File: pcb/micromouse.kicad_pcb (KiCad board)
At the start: 2 copper layers, 50 x 79.6 mm, 14 parts, among them J1 AVR-ISP-6, U1 TSSP77038ETR, U2 TSSP77038ETR, U3 TSSP77038ETR, U4 TSSP77038ETR, U5 TSSP77038ETR, U6 TSSP77038ETR, U7 ATmega328PB-A, Y1 Crystal

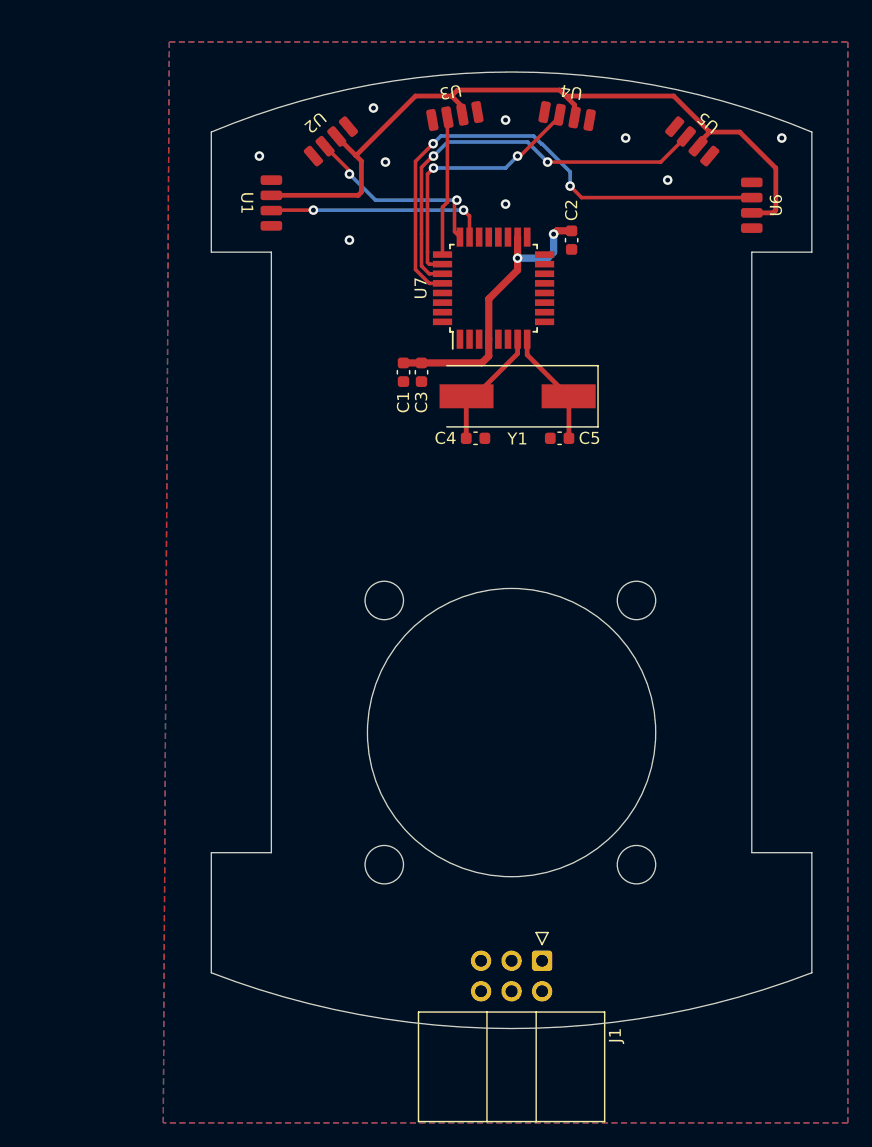
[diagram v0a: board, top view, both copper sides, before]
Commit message: add IR 3d + pin i2c screen
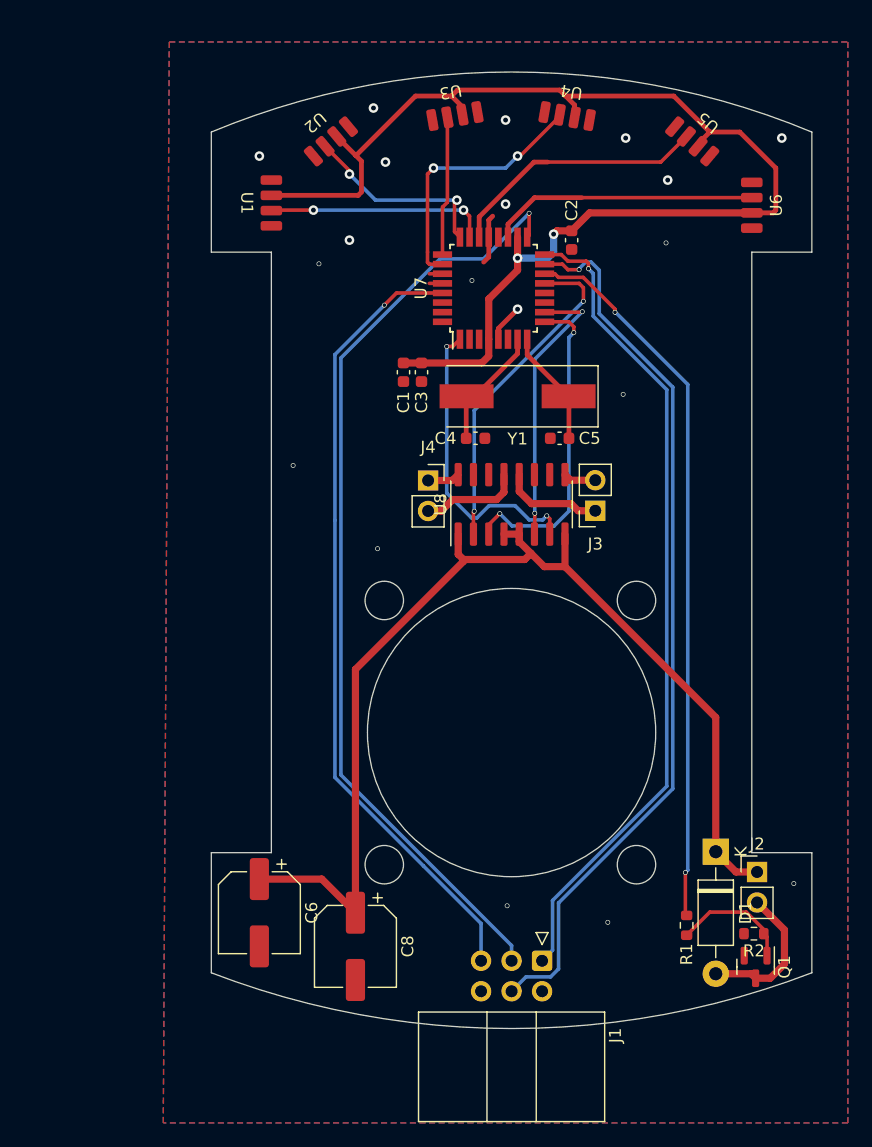
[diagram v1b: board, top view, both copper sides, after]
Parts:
- added C6: C_Polarized_Small, Capacitor_SMD:CP_Elec_6.3x4.9, F.Cu at (104.0, 95.0)
- added C8: C_Polarized_Small, Capacitor_SMD:CP_Elec_6.3x4.9, F.Cu at (112.0, 97.8)
- added D1: 1N5819, Diode_THT:D_DO-41_SOD81_P10.16mm_Horizontal, F.Cu at (142.0, 89.9)
- added J2: Conn_01x02, Connector_PinHeader_2.54mm:PinHeader_1x02_P2.54mm_Vertical, F.Cu at (145.4, 91.6)
- added J3: Conn_01x02, Connector_PinSocket_2.54mm:PinSocket_1x02_P2.54mm_Vertical, F.Cu at (132.0, 61.5)
- added J4: Conn_01x02, Connector_PinSocket_2.54mm:PinSocket_1x02_P2.54mm_Vertical, F.Cu at (118.0, 59.0)
- added Q1: Si2319CDS, Package_TO_SOT_SMD:SOT-23, F.Cu at (145.3, 99.5)
- added R1: R_Small, Resistor_SMD:R_0603_1608Metric, F.Cu at (139.6, 96.0)
- added R2: R_Small, Resistor_SMD:R_0603_1608Metric, F.Cu at (145.2, 96.7)
- added U8: MX1508, Package_SO:SOIC-16_3.9x9.9mm_P1.27mm, F.Cu at (125.0, 61.0)
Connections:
- U7 pad 14: unconnected-(U7-PB2-Pad14) -> MOTOR_1
- U7 pad 19: unconnected-(U7-PE2-Pad19) -> IR6
- U7 pad 22: unconnected-(U7-PE3-Pad22) -> IR5
- U7 pad 27: IR5 -> SDA
- U7 pad 28: IR6 -> SCL
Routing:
- net +BATT: track 0.00 -> 92.8 mm
- net SCK: track 0.00 -> 78.8 mm, vias 0 -> 1
- net MOSI: track 0.00 -> 74.7 mm, vias 0 -> 1
- net MISO: track 0.00 -> 69.0 mm, vias 0 -> 1
- net RST: track 0.00 -> 66.6 mm, vias 0 -> 1
- net MOTOR_1: track 0.00 -> 60.2 mm, vias 0 -> 2
- net MTR_L_1: track 0.00 -> 27.7 mm, vias 0 -> 2
- net MTR_L_2: track 0.00 -> 26.9 mm, vias 0 -> 2
- net MTR_R_2: track 0.00 -> 25.4 mm, vias 0 -> 2
- net MTR_R_1: track 0.00 -> 23.3 mm, vias 0 -> 2
- net IR6: track 43.4 -> 22.3 mm, vias 2 -> 0
- net +3.3V: track 88.8 -> 104.4 mm
- net IR5: track 34.7 -> 21.7 mm, vias 2 -> 0
- net Net-(D1-A): track 0.00 -> 12.4 mm
- net Net-(Q1-G): track 0.00 -> 10.1 mm
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
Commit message: remake IR wiring
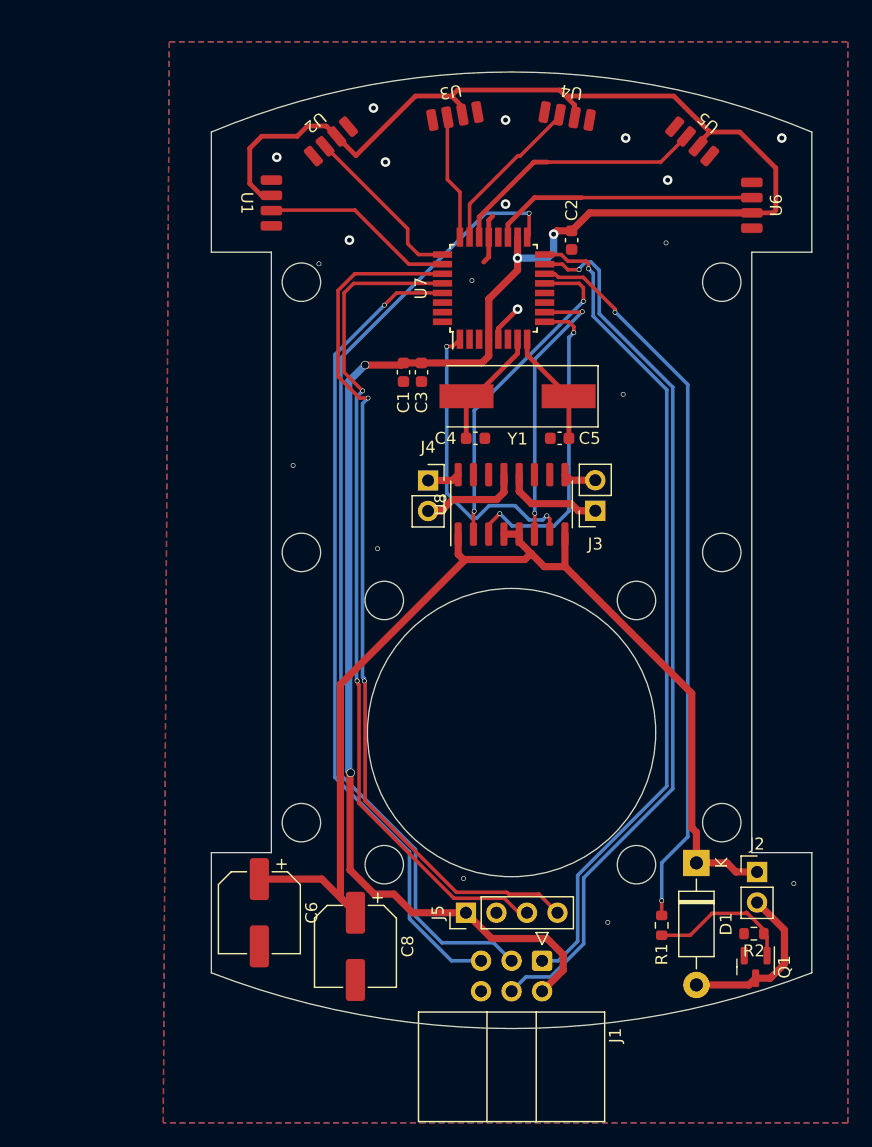
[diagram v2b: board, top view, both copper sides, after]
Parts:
- added J5: Conn_01x04, Connector_PinHeader_2.54mm:PinHeader_1x04_P2.54mm_Vertical, F.Cu at (121.2, 95.0)
- moved R1 2.07 mm to (137.5, 96.0)
- moved D1 1.86 mm to (140.4, 90.9)
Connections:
- U7 pad 23: IR1 -> IR4
- U7 pad 24: IR2 -> IR3
- U7 pad 25: IR3 -> IR2
- U7 pad 26: IR4 -> IR1
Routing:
- net +3.3V: track 104.4 -> 177.5 mm, vias 2 -> 4
- net SDA: track 1.10 -> 73.4 mm, vias 0 -> 2
- net SCL: track 1.10 -> 69.8 mm, vias 0 -> 2
- net IR4: track 21.8 -> 13.4 mm, vias 2 -> 0
- net +BATT: track 92.8 -> 95.3 mm
- net SCK: track 78.8 -> 81.3 mm
- net IR1: track 18.5 -> 16.1 mm, vias 2 -> 0
- net IR2: track 16.4 -> 14.2 mm, vias 2 -> 0
- net Net-(Q1-G): track 10.1 -> 12.2 mm
- net Net-(D1-A): track 12.4 -> 14.1 mm
- net RST: track 66.6 -> 68.0 mm
- net IR3: track 11.6 -> 10.4 mm
- net MISO: track 69.0 -> 69.8 mm
- net MOTOR_1: track 60.2 -> 61.0 mm
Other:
- outline, holes or cut-outs redrawn

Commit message: update link
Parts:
- added C10: 10u, Capacitor_SMD:C_0603_1608Metric, F.Cu at (115.0, 64.8)
- added C7: 10u, Capacitor_SMD:C_0603_1608Metric, F.Cu at (118.5, 64.8)
- added C9: 10u, Capacitor_SMD:C_0603_1608Metric, F.Cu at (116.5, 64.8)
- added J6: Conn_01x02, Connector_PinSocket_2.54mm:PinSocket_1x02_P2.54mm_Vertical, F.Cu at (135.0, 101.9)
- added U9: LM317_SOT-223, Package_TO_SOT_SMD:SOT-223-3_TabPin2, F.Cu at (112.5, 58.1)
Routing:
- net +3.3V: track 177.5 -> 192.0 mm, vias 4 -> 5
- net +BATT: track 95.3 -> 102.8 mm

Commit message: update output
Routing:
- net +BATT: track 102.8 -> 114.7 mm
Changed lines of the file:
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@@
       (plot_on_all_layers_selection 0x0000000_00000000)
       (disableapertmacros false)
-      (usegerberextensions false)
-      (usegerberattributes true)
-      (usegerberadvancedattributes true)
-      (creategerberjobfile true)
+      (usegerberextensions true)
+      (usegerberattributes false)
+      (usegerberadvancedattributes false)
+      (creategerberjobfile false)
       (dashed_line_dash_ratio 12.000000)
       (dashed_line_gap_ratio 3.000000)
@@
       (psa4output false)
       (plotreference true)
-      (plotvalue true)
+      (plotvalue false)
       (plotinvisibletext false)
       (sketchpadsonfab false)
-      (subtractmaskfromsilk false)
+      (subtractmaskfromsilk true)
       (outputformat 1)
       (mirror false)
-      (drillshape 1)
+      (drillshape 0)
       (scaleselection 1)
-      (outputdirectory "")
+      (outputdirectory "../cam/")
     )
   )
@@
     (fp_line (start 13.28 10.18) (end 4.38 10.18)
       (stroke (width 0.1) (type solid)) (layer "F.Fab"))
-    (pad "1" thru_hole roundrect (at 0 0 270) (size 1.7 1.7) (drill 1) (layers "*.Cu" "*.Mask") (roundrect_rratio 0.147059)
+    (pad "1" thru_hole roundrect (at 0 0 270) (size 1.7 1.7) (drill 1) (layers "*.Cu" "*.Mask") (roundrect_rratio 0.1470588235)
       (net 5 "MISO") (pinfunction "MISO") (pintype "passive"))
     (pad "2" thru_hole circle (at 2.54 0 270) (size 1.7 1.7) (drill 1) (layers "*.Cu" "*.Mask")
@@
   (segment (start 126.915 35.46) (end 130.83525 35.46) (width 0.4) (layer "F.Cu") (net 24))
   (segment (start 129.445 66.185) (end 129.445 63.475) (width 0.6) (layer "F.Cu") (net 28))
+  (segment (start 138.380716 90.854284) (end 140.389298 90.854284) (width 0.6) (layer "F.Cu") (net 28))
   (segment (start 117.425 62.9) (end 116.5 62.9) (width 0.6) (layer "F.Cu") (net 28))
   (segment (start 140 87.92) (end 140 76.74) (width 0.6) (layer "F.Cu") (net 28))
@@
   (segment (start 120.005 64.025) (end 120.555 63.475) (width 0.6) (layer "F.Cu") (net 28))
   (segment (start 116.5 62.9) (end 114.85 61.25) (width 0.6) (layer "F.Cu") (net 28))
+  (segment (start 135 94.235) (end 138.380716 90.854284) (width 0.6) (layer "F.Cu") (net 28))
   (segment (start 145.439832 91.606544) (end 143.686544 91.606544) (width 0.6) (layer "F.Cu") (net 28))
   (segment (start 118.55 64.025) (end 120.005 64.025) (width 0.6) (layer "F.Cu") (net 28))
@@
   (segment (start 109.2 92.2) (end 112 95) (width 0.6) (layer "F.Cu") (net 28))
   (segment (start 126.1 65.59) (end 126.612881 65.077119) (width 0.6) (layer "F.Cu") (net 28))
+  (segment (start 135 99.35) (end 135 94.235) (width 0.6) (layer "F.Cu") (net 28))
   (segment (start 125.635 63.475) (end 125.635 64.885) (width 0.6) (layer "F.Cu") (net 28))
   (segment (start 120.99 65.75) (end 120.99 65.59) (width 0.6) (layer "F.Cu") (net 28))

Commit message: leds placed
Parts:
- removed U1, U2, U3, U4, U5, U6: TSSP77038ETR, Library:TSSP77
- added D10: TSAL4400, LED_THT:LED_D3.0mm_IRBlack, F.Cu at (138.8, 30.5)
- added D11: TSAL4400, LED_THT:LED_D3.0mm_IRBlack, F.Cu at (143.8, 30.5)
- added D12: TSAL4400, LED_THT:LED_D3.0mm_IRBlack, F.Cu at (147.5, 33.8)
- added D13: TSAL4400, LED_THT:LED_D3.0mm_IRBlack, F.Cu at (147.5, 38.8)
- added D2: TSAL4400, LED_THT:LED_D3.0mm_IRBlack, F.Cu at (102.5, 33.8)
- added D3: TSAL4400, LED_THT:LED_D3.0mm_IRBlack, F.Cu at (102.5, 38.8)
- added D4: TSAL4400, LED_THT:LED_D3.0mm_IRBlack, F.Cu at (106.2, 30.8)
- added D5: TSAL4400, LED_THT:LED_D3.0mm_IRBlack, F.Cu at (111.2, 30.8)
- added D6: TSAL4400, LED_THT:LED_D3.0mm_IRBlack, F.Cu at (116.2, 28.0)
- added D7: TSAL4400, LED_THT:LED_D3.0mm_IRBlack, F.Cu at (121.2, 28.0)
- added D8: TSAL4400, LED_THT:LED_D3.0mm_IRBlack, F.Cu at (126.2, 28.0)
- added D9: TSAL4400, LED_THT:LED_D3.0mm_IRBlack, F.Cu at (131.2, 28.0)
- added R10: R_Small, Resistor_SMD:R_0603_1608Metric, F.Cu at (89.7, 31.0)
- added R11: R_Small, Resistor_SMD:R_0603_1608Metric, F.Cu at (93.7, 23.5)
- added R12: R_Small, Resistor_SMD:R_0603_1608Metric, F.Cu at (93.7, 26.0)
- added R13: R_Small, Resistor_SMD:R_0603_1608Metric, F.Cu at (93.7, 28.5)
- added R14: R_Small, Resistor_SMD:R_0603_1608Metric, F.Cu at (93.7, 31.0)
- added R3: R_Small, Resistor_SMD:R_0603_1608Metric, F.Cu at (85.7, 23.5)
- added R4: R_Small, Resistor_SMD:R_0603_1608Metric, F.Cu at (85.7, 26.0)
- added R5: R_Small, Resistor_SMD:R_0603_1608Metric, F.Cu at (85.7, 28.5)
- added R6: R_Small, Resistor_SMD:R_0603_1608Metric, F.Cu at (85.7, 31.0)
- added R7: R_Small, Resistor_SMD:R_0603_1608Metric, F.Cu at (89.7, 23.5)
- added R8: R_Small, Resistor_SMD:R_0603_1608Metric, F.Cu at (89.7, 26.0)
- added R9: R_Small, Resistor_SMD:R_0603_1608Metric, F.Cu at (89.7, 28.5)
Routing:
- net +3.3V: track 192.0 -> 111.6 mm
- net IR5: track 21.7 -> 1.68 mm
- net IR6: track 22.3 -> 4.21 mm
- net IR4: track 13.4 -> 2.75 mm
- net IR2: track 14.2 -> 4.51 mm
- net IR1: track 16.1 -> 9.16 mm
- net IR3: track 10.4 -> 3.75 mm
- net GND: vias 19 -> 12

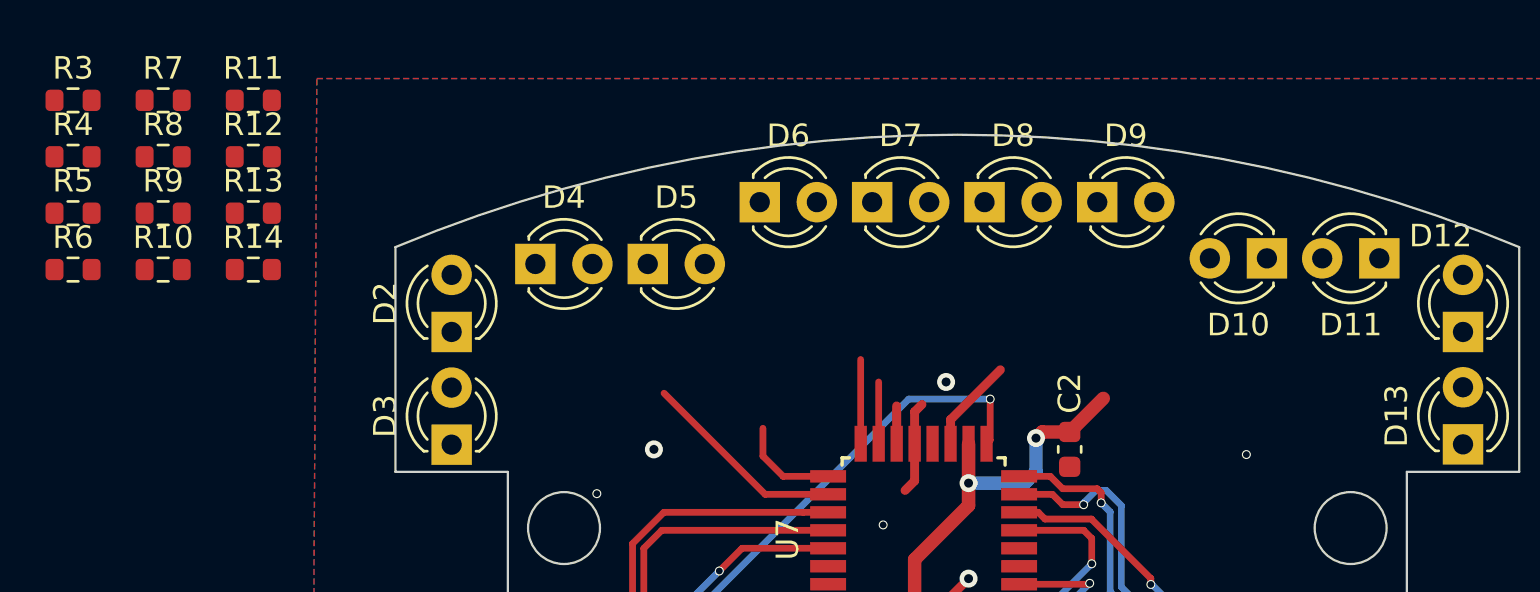
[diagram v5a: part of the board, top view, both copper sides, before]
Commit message: leds resistor placed
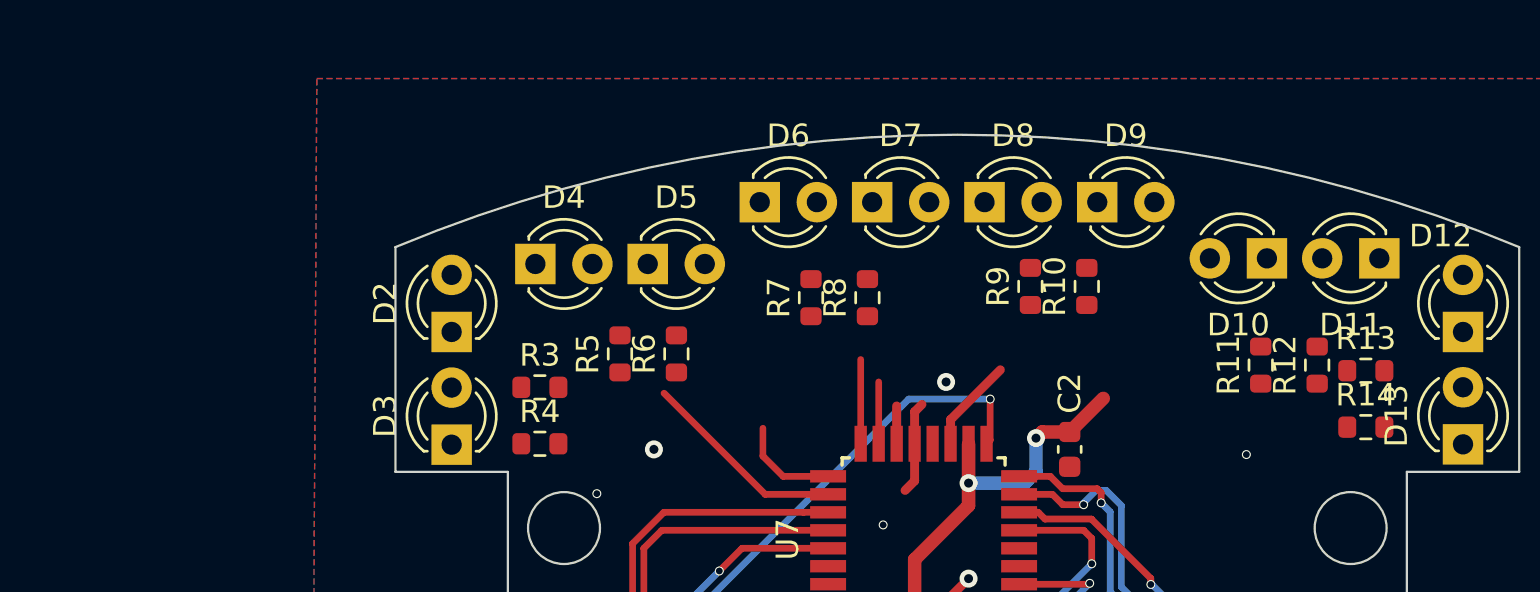
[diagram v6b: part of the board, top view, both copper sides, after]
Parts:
- moved R13 50.0 mm to (143.2, 35.5)
- moved R14 50.0 mm to (143.2, 38.0)
- moved R12 48.2 mm to (141.0, 35.2), turned to 90 degrees
- moved R11 46.3 mm to (138.5, 35.2), turned to 90 degrees
- moved R10 41.1 mm to (130.8, 31.8), turned to 90 degrees
- moved R9 38.7 mm to (128.2, 31.8), turned to 90 degrees
- moved R8 32.0 mm to (121.0, 32.2), turned to 90 degrees
- moved R7 30.1 mm to (118.5, 32.2), turned to 90 degrees
- moved R6 27.1 mm to (112.5, 34.8), turned to 90 degrees
- moved R5 25.1 mm to (110.0, 34.8), turned to 90 degrees
- moved R3 24.4 mm to (106.4, 36.2)
- moved R4 24.4 mm to (106.4, 38.8)

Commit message: finish wiring
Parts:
- moved R4 4.50 mm to (106.5, 34.2), turned to 180 degrees
- moved R11 2.37 mm to (136.2, 34.5)
- moved R12 1.91 mm to (139.2, 34.5)
- moved R3 0.76 mm to (106.5, 37.0), turned to 180 degrees
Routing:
- net +3.3V: track 111.6 -> 177.0 mm, vias 5 -> 8
- net IR6: track 4.21 -> 29.5 mm
- net IR5: track 1.68 -> 24.6 mm
- net IR4: track 2.75 -> 18.3 mm
- net IR3: track 3.75 -> 13.8 mm
- net IR1: track 9.16 -> 19.1 mm
- net IR2: track 4.51 -> 13.9 mm
- net Net-(D12-A): track 0.00 -> 5.71 mm
- net Net-(D2-A): track 0.00 -> 4.42 mm
- net Net-(D4-A): track 0.00 -> 3.69 mm
- net Net-(D6-A): track 0.00 -> 3.53 mm
- net Net-(D10-A): track 0.00 -> 3.18 mm
- net Net-(D8-A): track 0.00 -> 3.13 mm
- net GND: vias 12 -> 22
